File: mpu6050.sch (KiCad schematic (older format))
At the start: 5 parts, among them U2 MPU6050

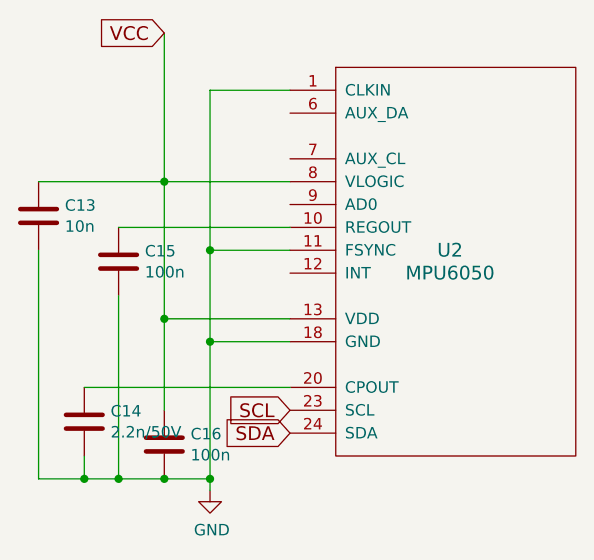
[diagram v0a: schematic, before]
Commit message: added i2c pullups, IMU int and USB sense
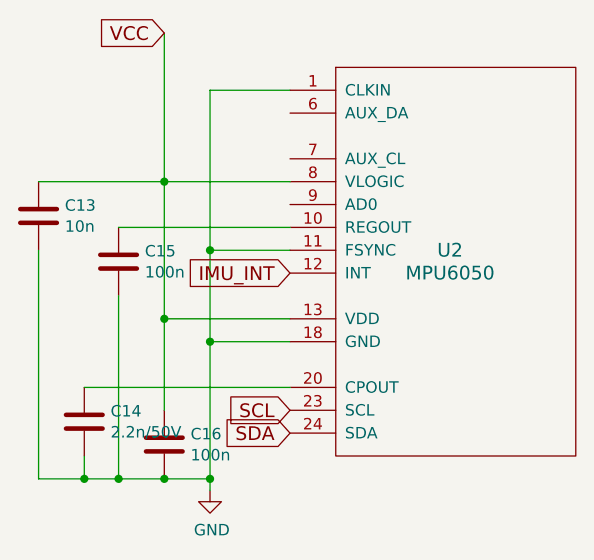
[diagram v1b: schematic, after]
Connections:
- net IMU_INT: now reaches U2.12 (INT)
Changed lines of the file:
@@
 LIBS:contrib
 LIBS:valves
-LIBS:minimal
 LIBS:alis_parts
 LIBS:stm32f4_lqfp64_mpu6050-cache
@@
 $EndComp
 $Comp
-L GND #PWR22
+L GND #PWR021
 U 1 1 569B8F29
 P 5450 4500
-F 0 "#PWR22" H 5450 4250 50  0001 C CNN
+F 0 "#PWR021" H 5450 4250 50  0001 C CNN
 F 1 "GND" H 5458 4326 50  0000 C CNN
 F 2 "" H 5450 4500 50  0000 C CNN
@@
 	1    0    0    -1
 $EndComp
+Text GLabel 5800 3550 0    60   Input ~ 0
+IMU_INT
 $EndSCHEMATC
